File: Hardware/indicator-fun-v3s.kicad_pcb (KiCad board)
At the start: 2 copper layers, 100 x 100 mm, 159 parts, among them IC1 LM1117, J1 TRANSFLASH-LOCK, J2 AUDIO_JACK_SMD, J3 USB_B_Micro OTG, J4 Power, Q1 24Mhz, Q2 32kHz, SW1 Reset, SW2 BOOT, U1 25F32006WSOI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

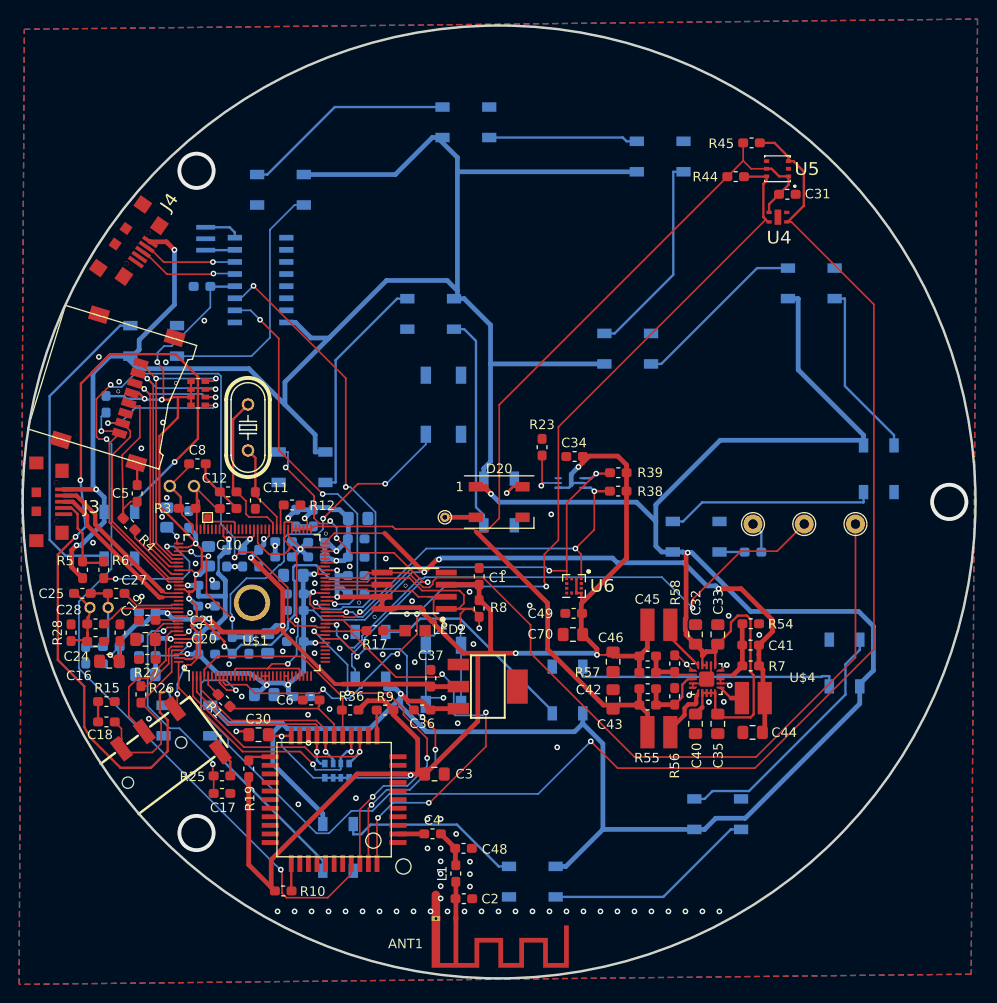
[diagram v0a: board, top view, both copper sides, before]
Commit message: SPI подсоединен к цепочке светодиодов и установлен транзистор разрешающий управление цепочкой по CS2
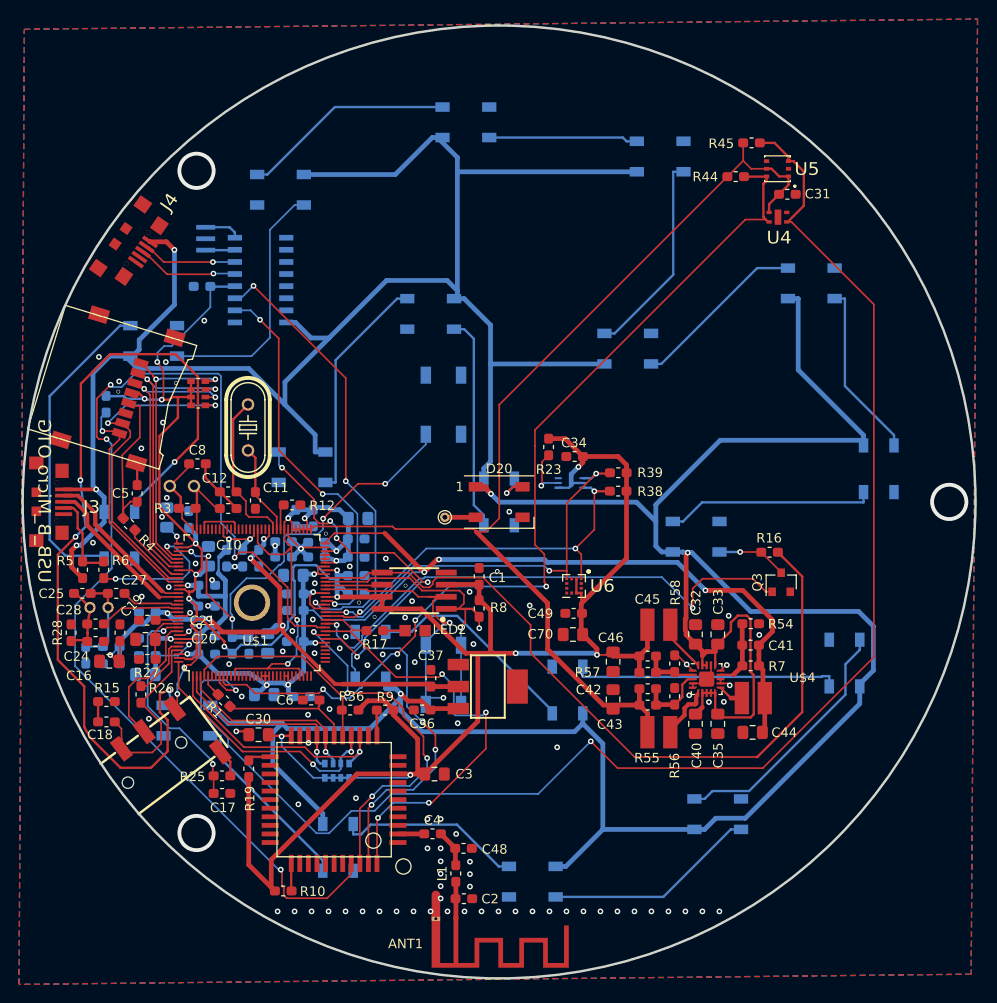
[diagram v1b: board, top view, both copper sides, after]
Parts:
- removed TP2: TestPoint, indicator-fun-v3s:TestPoint_Pad_1.0x1.0mm
- removed TP3: SPI LED Out, TestPoint:TestPoint_THTPad_D2.0mm_Drill1.0mm
- removed TP4: PWM LED Out, TestPoint:TestPoint_THTPad_D2.0mm_Drill1.0mm
- removed TP5: RGB IN CTL, TestPoint:TestPoint_THTPad_D2.0mm_Drill1.0mm
- added Q3: BSS138, Package_TO_SOT_SMD:SOT-23, F.Cu at (177.0, 103.9)
- R16: moved to F.Cu
- moved R16 1.74 mm to (175.8, 100.8)
- moved R23 0.69 mm to (152.6, 89.8), turned to 270 degrees
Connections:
- R16 pad 1: /Leds/RGB CTL -> LED_CTL
- R23 pad 1: /Sensors/Light-Int -> +3V3
- R23 pad 2: Net-(R23-Pad2) -> /Sensors/Light-Int
- U$1 pad 43: /WLAN/PB4/PWM0 -> CS2
- U$1 pad 55: /WLAN/SPI1/MOSI -> LED_CTL
- U1 pad 5: /WLAN/SPI1/MOSI -> LED_CTL
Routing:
- net /WLAN/SPI1/MOSI: track 85.0 -> 0.00 mm
- net LED_CTL: track 0.00 -> 80.9 mm
- net /WLAN/PB4/PWM0: track 60.8 -> 0.00 mm, vias 2 -> 0
- net CS2: track 0.00 -> 56.2 mm, vias 0 -> 2
- net Net-(D1-Pad4): track 2.65 -> 7.47 mm, vias 0 -> 1
- net +3V3: track 288.6 -> 292.2 mm
- net /Leds/RGB CTL: track 3.31 -> 0.00 mm
- net SCL-1.8: track 97.7 -> 99.5 mm
- net Net-(C24-Pad2): track 10.1 -> 8.32 mm
- net /Power/x32kout: track 9.54 -> 8.39 mm
- net /Power/for_delete: track 5.70 -> 4.70 mm
- net +1V2: track 153.1 -> 152.3 mm
- net Net-(D16-Pad2): track 38.8 -> 38.1 mm
- net /WLAN/UART2/CTS/PB3: track 121.9 -> 122.4 mm
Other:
- net class Default: clearance 0.2 -> 0.127
- rule trace_clearance: 0.2 -> 0.127

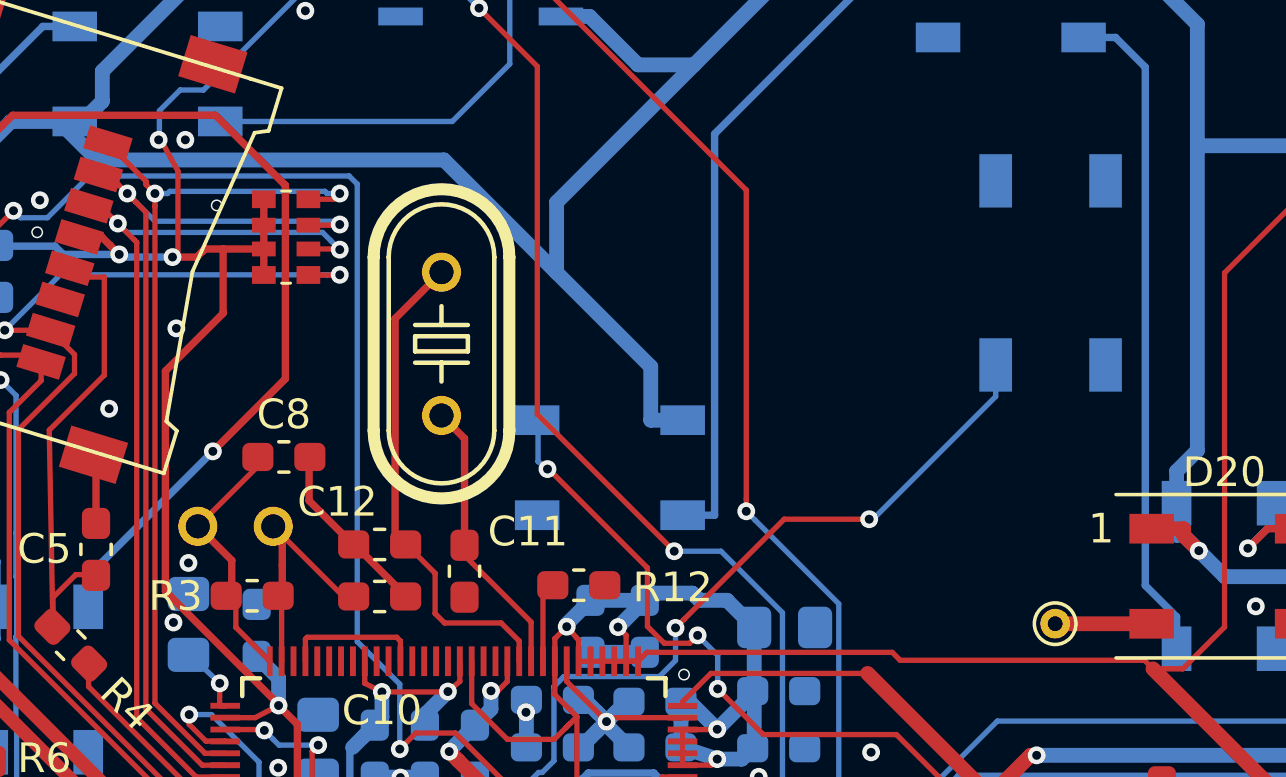
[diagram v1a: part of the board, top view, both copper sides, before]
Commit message: Заменены кварцы
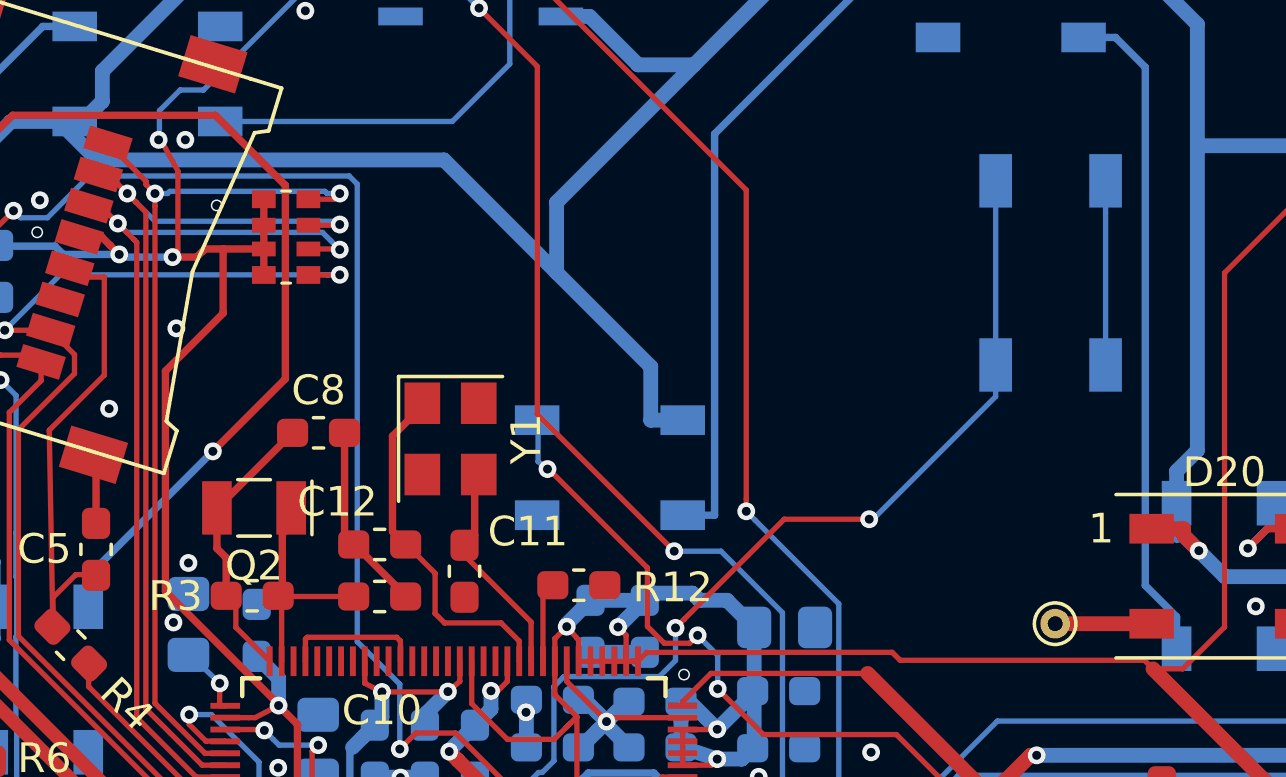
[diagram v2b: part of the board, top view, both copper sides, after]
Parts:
- removed Q1: 24Mhz, indicator-fun-v3s:HC49U-V
- added Y1: Crystal_GND24_Small, Crystal:Crystal_SMD_SeikoEpson_FA238V-4Pin_3.2x2.5mm, F.Cu at (121.3, 90.9)
- Q2: footprint indicator-fun-v3s:TC38H -> Crystal:Crystal_SMD_MicroCrystal_CC7V-T1A-2Pin_3.2x1.5mm; moved to F.Cu
- moved C8 1.42 mm to (116.9, 90.7)
- moved Q2 0.88 mm to (114.7, 93.2)
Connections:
- IC1 pad 4: /Power/+3V3ANC -> (no net)
- J4 pad 4: Net-(J4-Pad4) -> (no net)
- SW1 pad 2: Net-(SW1-Pad2) -> GND
- SW1 pad 4: Net-(SW1-Pad4) -> Net-(C13-Pad1)
- U$1 pad 10: /WLAN/MIPI-CSI-MCLK -> (no net)
- U$1 pad 11: /WLAN/LCD_D21 -> (no net)
- U$1 pad 112: Net-(U$1-Pad112) -> (no net)
- U$1 pad 13: /WLAN/LCD_D20 -> (no net)
- U$1 pad 14: /WLAN/LCD_D19 -> (no net)
- U$1 pad 15: /WLAN/CSI_D12/LCD_D18 -> (no net)
- U$1 pad 16: /WLAN/CSI_D11/LCD_D15 -> (no net)
- U$1 pad 17: /WLAN/CSI_D10/LCD_D14 -> (no net)
- U$1 pad 18: /WLAN/CSI_D9/LCD_D13 -> (no net)
- U$1 pad 22: /WLAN/CSI_D8/LCD_D12 -> (no net)
- U$1 pad 23: /WLAN/CSI_D7/LCD_D11 -> (no net)
- U$1 pad 24: /WLAN/CSI_D6/LCD_D10 -> (no net)
- U$1 pad 27: /WLAN/CSI_D5/LCD_D7 -> (no net)
- U$1 pad 28: /WLAN/CSI_D4/LCD_D6 -> (no net)
- U$1 pad 30: /WLAN/CSI_D3/LCD_D5 -> (no net)
- U$1 pad 31: /WLAN/CSI_D2/LCD_D4 -> (no net)
- U$1 pad 32: /WLAN/CSI_D1/LCD_D3 -> (no net)
- U$1 pad 33: /WLAN/CSI_D0/LCD_D2 -> (no net)
- U$1 pad 34: /WLAN/CSI_VSYNC/LCD_VSYNC -> (no net)
- U$1 pad 35: /WLAN/CSI_HSYNC/LCD_HSYNC -> (no net)
- U$1 pad 36: /WLAN/CSI_MCLK/LCD_DE -> (no net)
- U$1 pad 37: /WLAN/CSI_PCLK/LCD_CLK -> (no net)
- U$1 pad 6: /WLAN/LCD_D23 -> (no net)
- U$1 pad 7: /WLAN/LCD_D22 -> (no net)
- U$1 pad 77: /USB-SDC0-Audio/LINK_LED -> (no net)
- U$1 pad 78: /USB-SDC0-Audio/SPD_LED -> (no net)
- U$1 pad 81: /USB-SDC0-Audio/MCSI-D0P -> (no net)
- U$1 pad 82: /USB-SDC0-Audio/MCSI-D0N -> (no net)
- U$1 pad 83: /USB-SDC0-Audio/MCSI-D1P -> (no net)
- U$1 pad 84: /USB-SDC0-Audio/MCSI-D1N -> (no net)
- U$1 pad 86: /USB-SDC0-Audio/MCSI-CKP -> (no net)
- U$1 pad 87: /USB-SDC0-Audio/MCSI-CKN -> (no net)
- U$1 pad 89: /USB-SDC0-Audio/EPHY_RXN -> (no net)
- U$1 pad 90: /USB-SDC0-Audio/EPHY_RXP -> (no net)
- U$1 pad 91: /USB-SDC0-Audio/EPHY_TXN -> (no net)
- U$1 pad 92: /USB-SDC0-Audio/EPHY_TXP -> (no net)
- U$1 pad 94: Net-(U$1-Pad94) -> (no net)
- U$2 pad P$10: Net-(U$2-PadP$10) -> (no net)
- U$2 pad P$11: Net-(U$2-PadP$11) -> (no net)
- U$2 pad P$13: /WLAN/WL_H_WK -> (no net)
- U$2 pad P$21: Net-(U$2-PadP$21) -> (no net)
- U$2 pad P$24: Net-(U$2-PadP$24) -> (no net)
- U$2 pad P$25: Net-(U$2-PadP$25) -> (no net)
- U$2 pad P$26: Net-(U$2-PadP$26) -> (no net)
- U$2 pad P$27: Net-(U$2-PadP$27) -> (no net)
- U$2 pad P$28: Net-(U$2-PadP$28) -> (no net)
- U$2 pad P$29: Net-(U$2-PadP$29) -> (no net)
- U$2 pad P$30: Net-(U$2-PadP$30) -> (no net)
- U$2 pad P$32: Net-(U$2-PadP$32) -> (no net)
- U$2 pad P$35: Net-(U$2-PadP$35) -> (no net)
- U$2 pad P$37: Net-(U$2-PadP$37) -> (no net)
- U$2 pad P$38: Net-(U$2-PadP$38) -> (no net)
- U$2 pad P$39: Net-(U$2-PadP$39) -> (no net)
- U$2 pad P$4: Net-(U$2-PadP$4) -> (no net)
- U$2 pad P$40: Net-(U$2-PadP$40) -> (no net)
- U$2 pad P$5: Net-(U$2-PadP$5) -> (no net)
- U$2 pad P$6: /WLAN/BT_WK -> (no net)
- U$2 pad P$7: /WLAN/BT_H_WK -> (no net)
- U$2 pad P$8: Net-(U$2-PadP$8) -> (no net)
- U2 pad 10: Net-(U2-Pad10) -> (no net)
- U2 pad 11: Net-(U2-Pad11) -> (no net)
- U2 pad 12: Net-(U2-Pad12) -> (no net)
- U2 pad 13: Net-(U2-Pad13) -> (no net)
- U2 pad 14: Net-(U2-Pad14) -> (no net)
- U2 pad 15: Net-(U2-Pad15) -> (no net)
- U2 pad 9: Net-(U2-Pad9) -> (no net)
- U6 pad 11: /Sensors/Accel-Int1 -> (no net)
- U6 pad 12: /Sensors/Accel-Int2 -> (no net)
- U6 pad 3: Net-(U6-Pad3) -> (no net)
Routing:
- net GND: track 27.6 -> 34.1 mm
- net Net-(C13-Pad1): track 47.6 -> 53.8 mm
- net /Power/x24min: track 16.6 -> 12.5 mm
- net /Power/x24mount: track 9.52 -> 7.42 mm
- net /Power/x32kin: track 8.99 -> 9.60 mm

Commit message: Версия 1.1 Отправлена в производство
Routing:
- net /WLAN/UART2/RTS/PB2: track 45.6 -> 46.6 mm
- net +5V: track 459.6 -> 460.2 mm
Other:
- board text added: "Ver. 1.1 www.indicator.fun"
- board text removed: "V1.0 Alex Vrubel Moscow 2019"

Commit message: Добавлен усилитель, но не сделана трассировка дорожек
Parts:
- added AOut_1: AOut_1, TestPoint:TestPoint_THTPad_D1.5mm_Drill0.7mm, F.Cu at (149.3, 74.1)
- added AOut_2: AOut_2, TestPoint:TestPoint_THTPad_D1.5mm_Drill0.7mm, F.Cu at (149.3, 84.7)
- added C73: 100nF, Capacitor_SMD:C_0603_1608Metric_Pad1.05x0.95mm_HandSolder, F.Cu at (136.1, 77.9)
- added C74: 100nF, Capacitor_SMD:C_0603_1608Metric_Pad1.05x0.95mm_HandSolder, F.Cu at (149.5, 80.0)
- added C75: 10µF, Capacitor_SMD:C_0805_2012Metric_Pad1.15x1.40mm_HandSolder, F.Cu at (152.5, 80.1)
- added C76: 100nF, Capacitor_SMD:C_0603_1608Metric_Pad1.05x0.95mm_HandSolder, F.Cu at (136.1, 81.6)
- added IC2: MD8002A, indicator-fun-v3s:SOIC127P600X175-8N, F.Cu at (142.8, 78.5)
- added R18: 10k, Resistor_SMD:R_0603_1608Metric_Pad1.05x0.95mm_HandSolder, F.Cu at (135.2, 87.0)
- added R20: 22k, Resistor_SMD:R_0603_1608Metric_Pad1.05x0.95mm_HandSolder, F.Cu at (142.7, 83.9)
- added R21: 10k, Resistor_SMD:R_0603_1608Metric_Pad1.05x0.95mm_HandSolder, F.Cu at (135.1, 84.8)
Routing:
- net Net-(AOut_2-Pad1): track 0.00 -> 10.5 mm
- net +3V3A: track 63.5 -> 70.5 mm
- net Net-(AOut_1-Pad1): track 0.00 -> 4.84 mm
- net Net-(C76-Pad2): track 0.00 -> 4.82 mm
- net Net-(C73-Pad2): track 0.00 -> 4.41 mm
- net GND: vias 104 -> 106

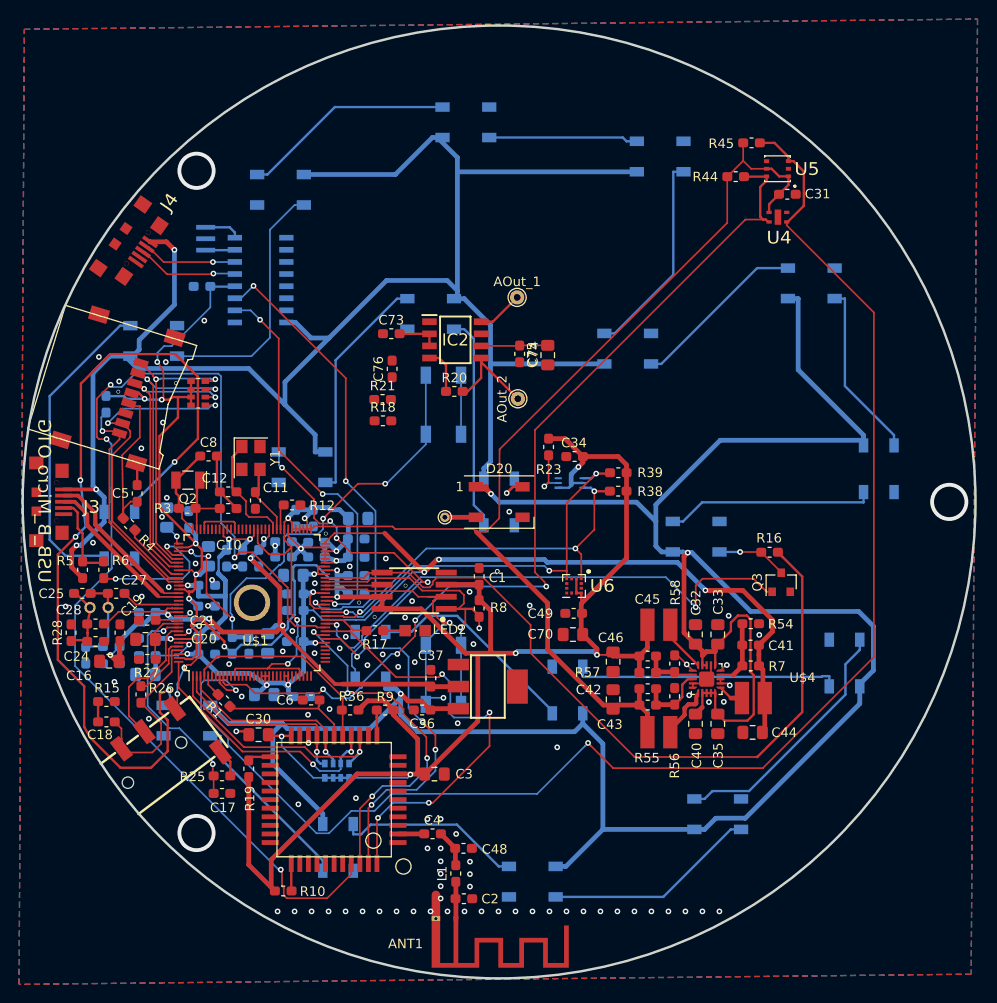
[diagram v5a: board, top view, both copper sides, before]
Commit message: Разведены две дорожки звука на усилитель
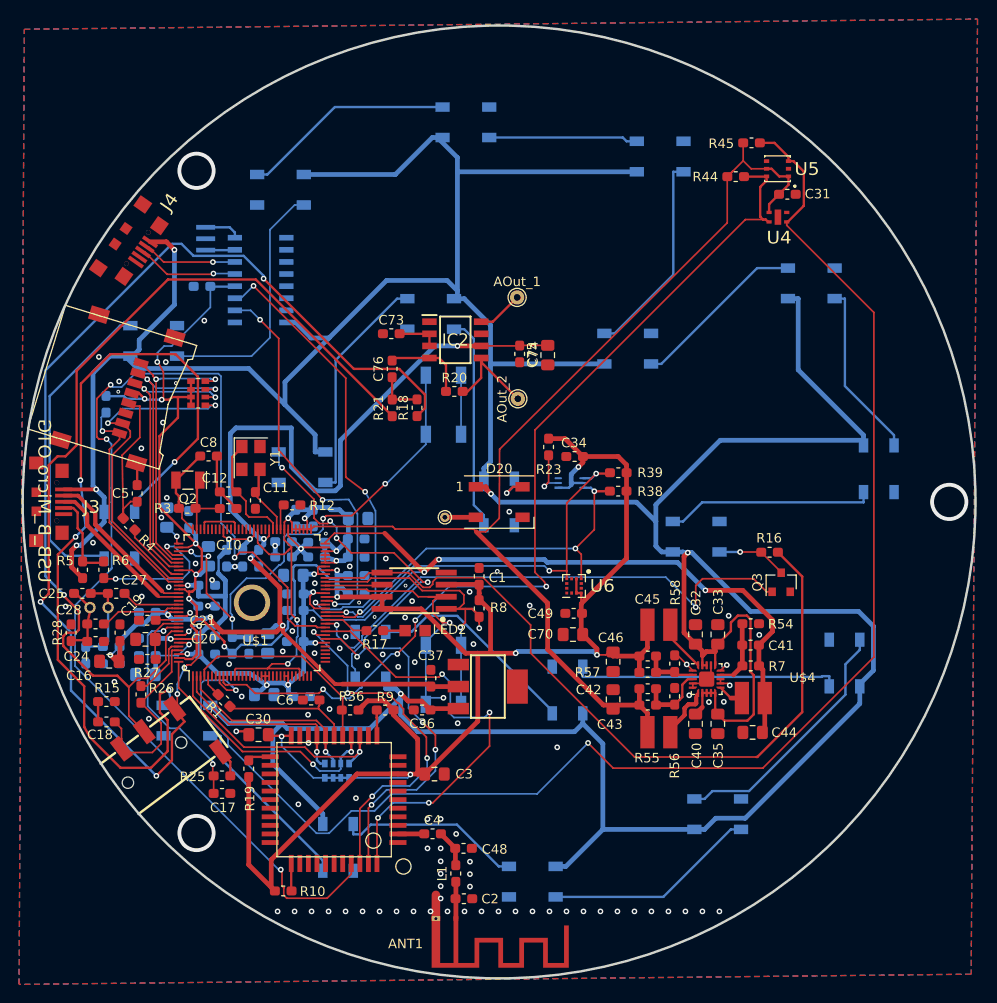
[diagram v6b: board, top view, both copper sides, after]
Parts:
- moved R18 3.83 mm to (138.8, 85.6), turned to 90 degrees
- moved R21 1.34 mm to (136.2, 85.6), turned to 90 degrees
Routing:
- net /USB-SDC0-Audio/HP_L: track 12.5 -> 113.8 mm, vias 4 -> 6
- net /USB-SDC0-Audio/HP_R: track 14.4 -> 109.4 mm, vias 0 -> 2
- net +3V3A: track 70.5 -> 124.7 mm, vias 6 -> 7
- net Net-(C76-Pad1): track 0.00 -> 4.95 mm
- net Net-(C76-Pad2): track 4.82 -> 8.85 mm
- net +3V3: track 292.4 -> 293.7 mm
- net +1V8: track 177.0 -> 177.8 mm
- net /Power/x32kin: track 9.60 -> 10.3 mm
- net SDA-1.8: track 157.8 -> 158.5 mm
- net /WLAN/SPI1/CS: track 32.5 -> 33.0 mm
